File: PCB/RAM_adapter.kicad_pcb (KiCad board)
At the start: 2 copper layers, 78 x 64.5 mm, 18 parts, among them J1 #WR, J2 DB25_Plug, U1 HM62256BLP, U2 74LS573

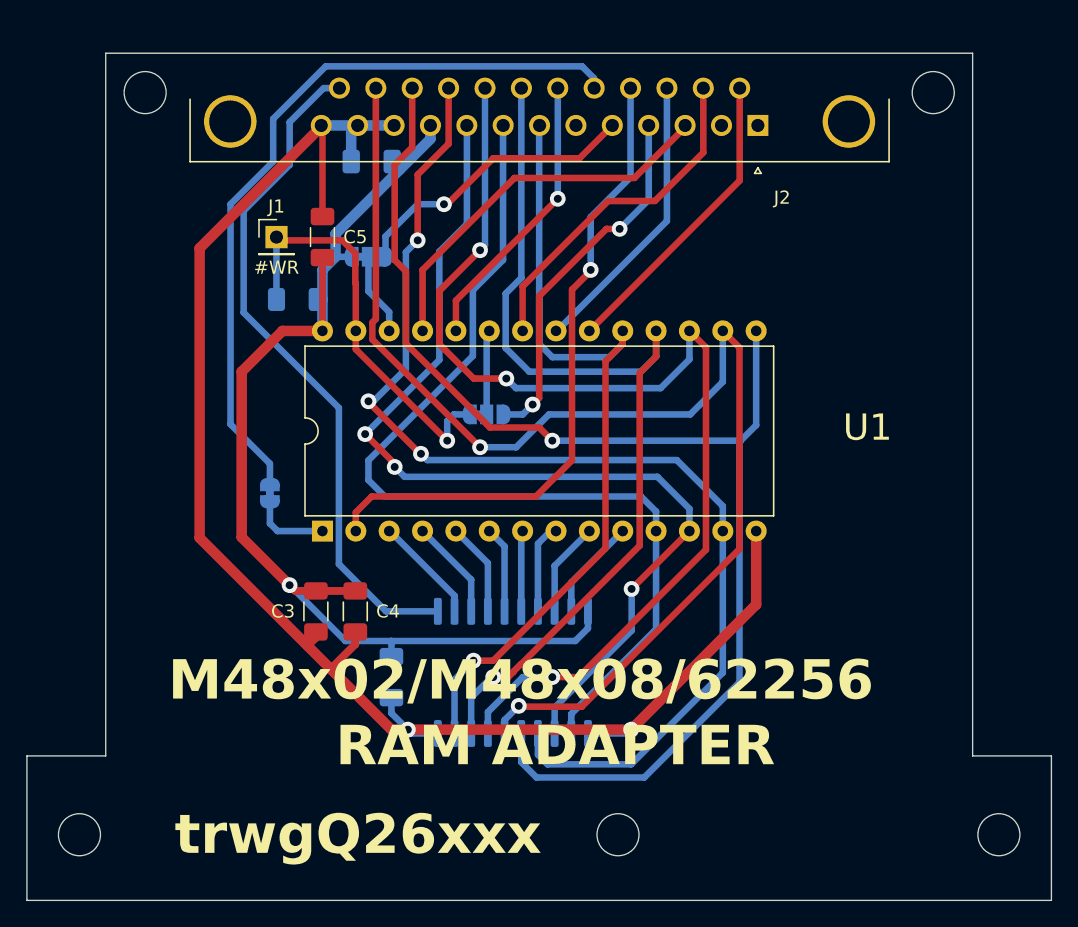
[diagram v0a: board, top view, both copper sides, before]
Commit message: Revised RAM adapter PCB
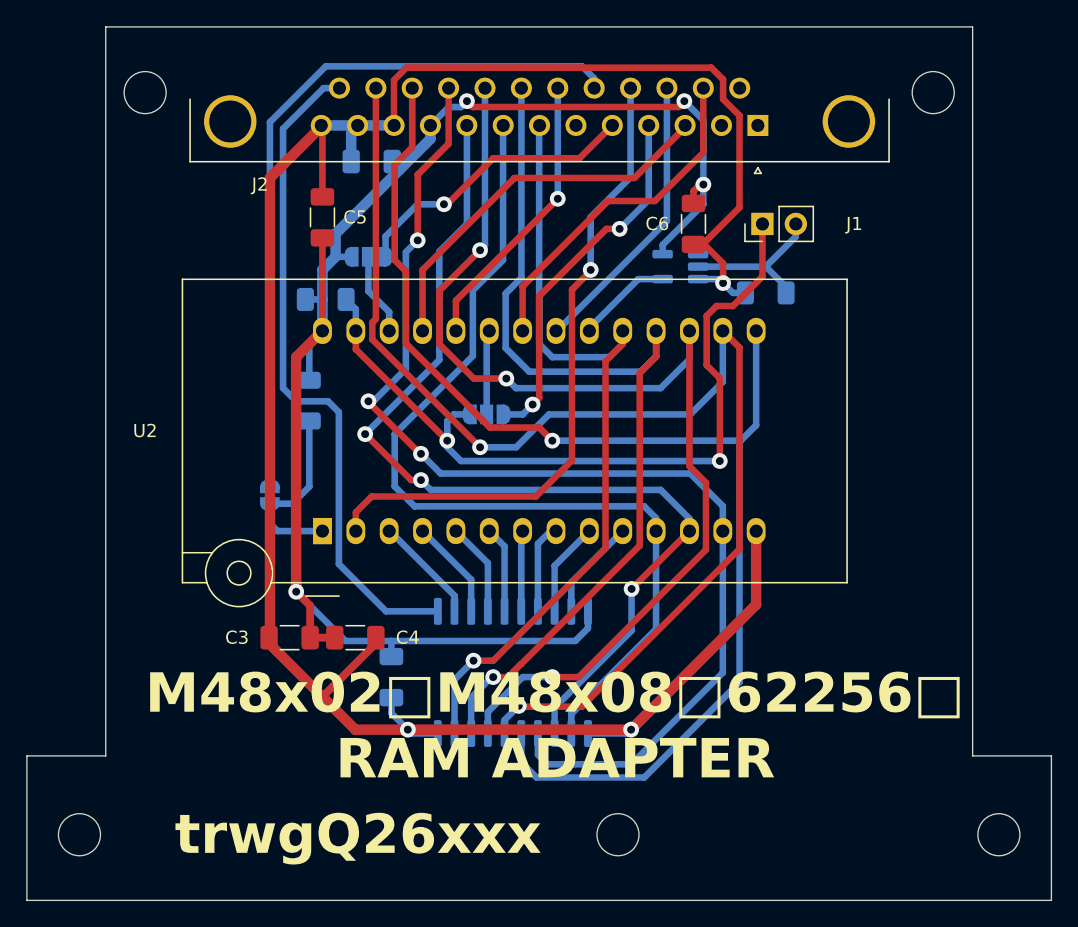
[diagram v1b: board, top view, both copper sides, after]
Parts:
- added C6: 100n, Capacitor_SMD:C_1206_3216Metric_Pad1.33x1.80mm_HandSolder, F.Cu at (166.8, 35.5)
- added R2: 10k, Resistor_SMD:R_1206_3216Metric_Pad1.30x1.75mm_HandSolder, B.Cu at (172.2, 40.8)
- added R3: 10k, Resistor_SMD:R_1206_3216Metric_Pad1.30x1.75mm_HandSolder, B.Cu at (137.5, 49.0)
- added U1: 74LVC1G04, Package_TO_SOT_SMD:SOT-23-5_HandSoldering, B.Cu at (165.8, 38.8)
- J1: value #WR -> EC; footprint Connector_PinHeader_2.54mm:PinHeader_1x01_P2.54mm_Vertical -> Connector_PinHeader_2.54mm:PinHeader_1x02_P2.54mm_Vertical
- JP1: footprint Jumper:SolderJumper-2_P1.3mm_Bridged_RoundedPad1.0x1.5mm -> Jumper:SolderJumper-2_P1.3mm_Open_RoundedPad1.0x1.5mm
- JP2, JP3: footprint Jumper:SolderJumper-3_P1.3mm_Bridged12_RoundedPad1.0x1.5mm_NumberLabels -> Jumper:SolderJumper-3_P1.3mm_Open_RoundedPad1.0x1.5mm
- U2: renamed from U1; footprint Package_DIP:DIP-28_W15.24mm -> Socket:DIP_Socket-28_W11.9_W12.7_W15.24_W17.78_W18.5_3M_228-1277-00-0602J
- moved J1 37.0 mm to (172.0, 35.5), turned to 90 degrees
- moved C3 2.83 mm to (136.0, 67.0), turned to 180 degrees
- moved R1 2.20 mm to (138.8, 41.2), turned to 0 degrees
- moved C4 2.00 mm to (141.0, 67.0), turned to 0 degrees
- moved C5 1.50 mm to (138.5, 35.0)
- moved JP1 0.15 mm to (134.5, 56.1)
- renumbered U2 to U3
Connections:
- J2 pad 14: #A -> unconnected-(J2-P14-Pad14)
- U2 pad 20: #A -> #CS
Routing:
- net GND: track 122.8 -> 171.4 mm, vias 2 -> 3
- net +5V: track 84.9 -> 122.7 mm, vias 1 -> 4
- net #WR: track 31.8 -> 60.3 mm, vias 1 -> 2
- net #A: track 23.2 -> 0.00 mm
- net A15: track 0.00 -> 12.0 mm
- net Net-(JP1-A): track 5.89 -> 14.4 mm
- net #CS: track 0.00 -> 7.34 mm
- net /D0: track 73.7 -> 70.9 mm
- net /A14: track 57.7 -> 55.2 mm
- net AS: track 52.0 -> 50.9 mm
- net /D1: track 75.3 -> 74.7 mm
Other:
- board size 78 x 64.5 mm -> 78 x 66.5 mm
- board text added: "M48x02□M48x08□62256□"
- board text added: "MT48x02/MT48x12: JP1 Don't care, JP2 1-2, JP3 1-2 MT48x08/MT48x18: JP1 OFF, JP2 1-2, JP3 2-3 62256: JP1 ON, JP2 2-3, JP3 2-3"
- board text removed: "M48x02/M48x08/62256"
- board text removed: "MT48x02/MT48x12: JP1 Don't care,JP2 1-2, JP3 1-2 MT48x08/MT48x18: JP1 OFF, JP2 1-2, JP3 2-3 62256: JP1 ON, JP2 2-3, JP3 2-3"

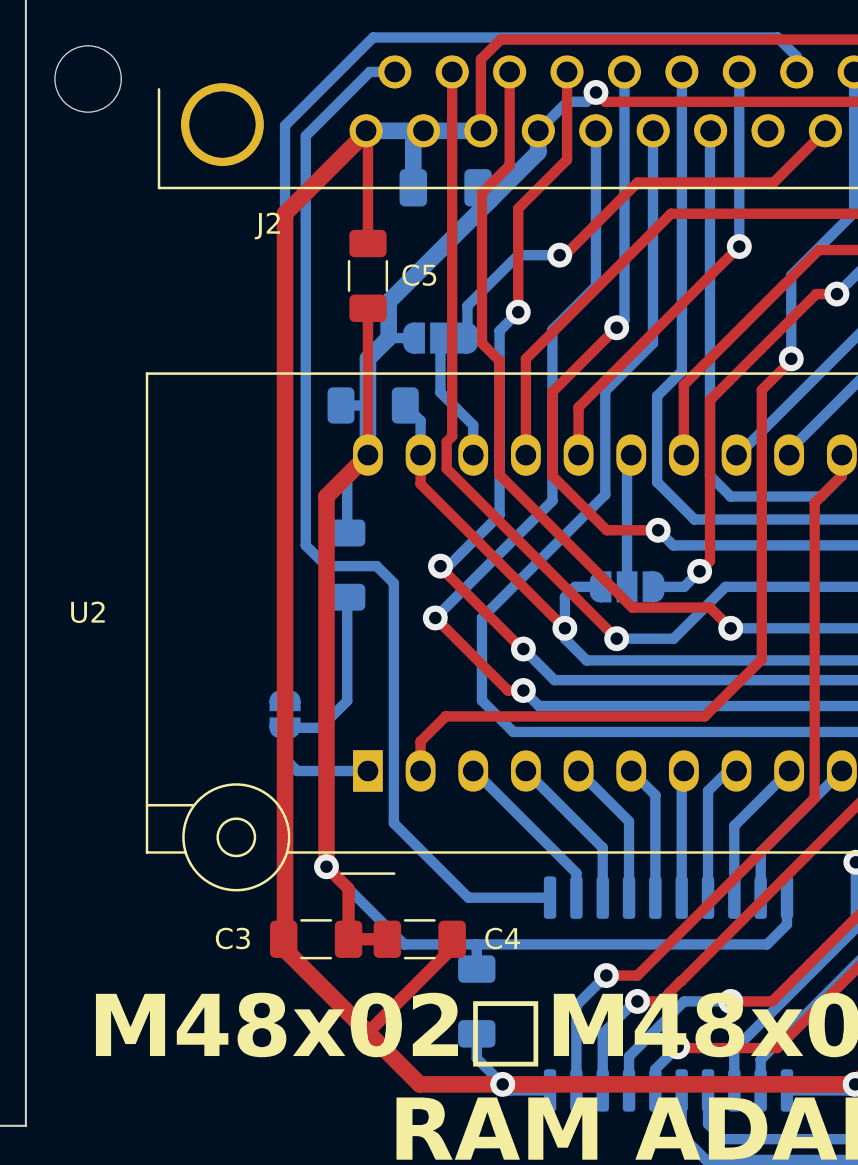
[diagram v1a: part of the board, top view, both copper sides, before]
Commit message: ROM reader project PCBs updated
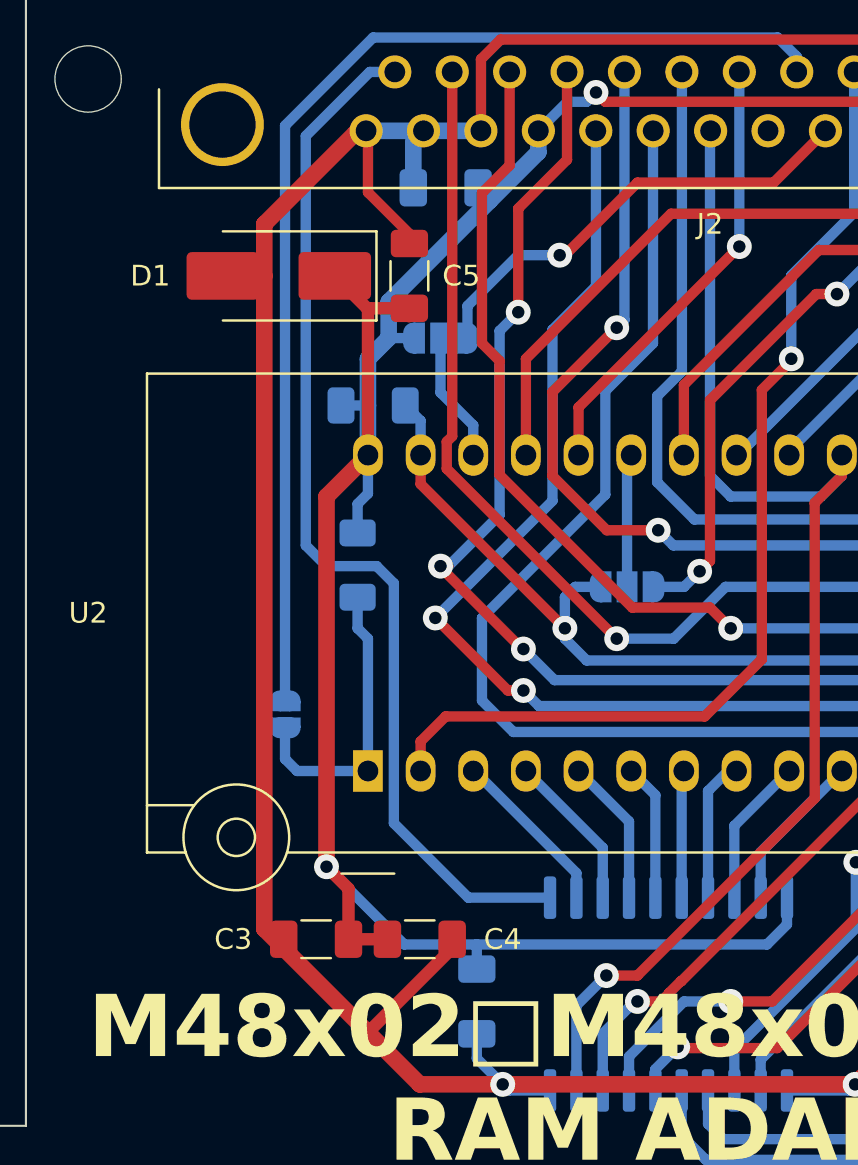
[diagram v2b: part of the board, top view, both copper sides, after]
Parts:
- added D1: Schottky, Diode_SMD:D_SMB_Handsoldering, F.Cu at (134.2, 35.0)
- moved C5 2.00 mm to (140.5, 35.0)
- moved R3 0.50 mm to (138.0, 49.0)
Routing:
- net +5V: track 122.7 -> 127.2 mm
- net GND: track 171.4 -> 175.4 mm
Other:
- board text added: "M48x02/M48x12: JP1 OFF, JP2 1-2, JP3 1-2 M48x08/M48x18: JP1 OFF, JP2 1-2, JP3 2-3 62256: JP1 ON, JP2 2-3, JP3 2-3"
- board text removed: "MT48x02/MT48x12: JP1 Don't care, JP2 1-2, JP3 1-2 MT48x08/MT48x18: JP1 OFF, JP2 1-2, JP3 2-3 62256: JP1 ON, JP2 2-3, JP3 2-3"

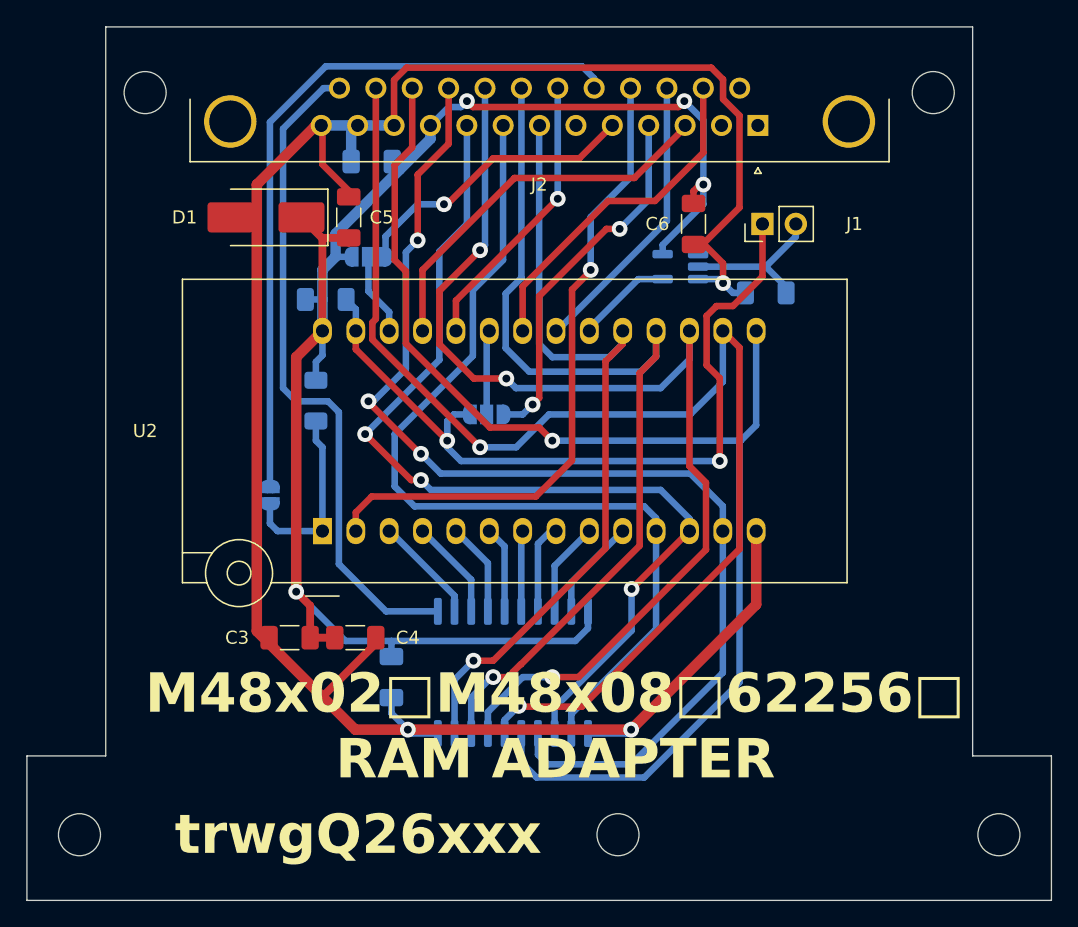
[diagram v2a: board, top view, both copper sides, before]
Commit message: Minor changes in text placement on PCB, comments. Revision updated to B
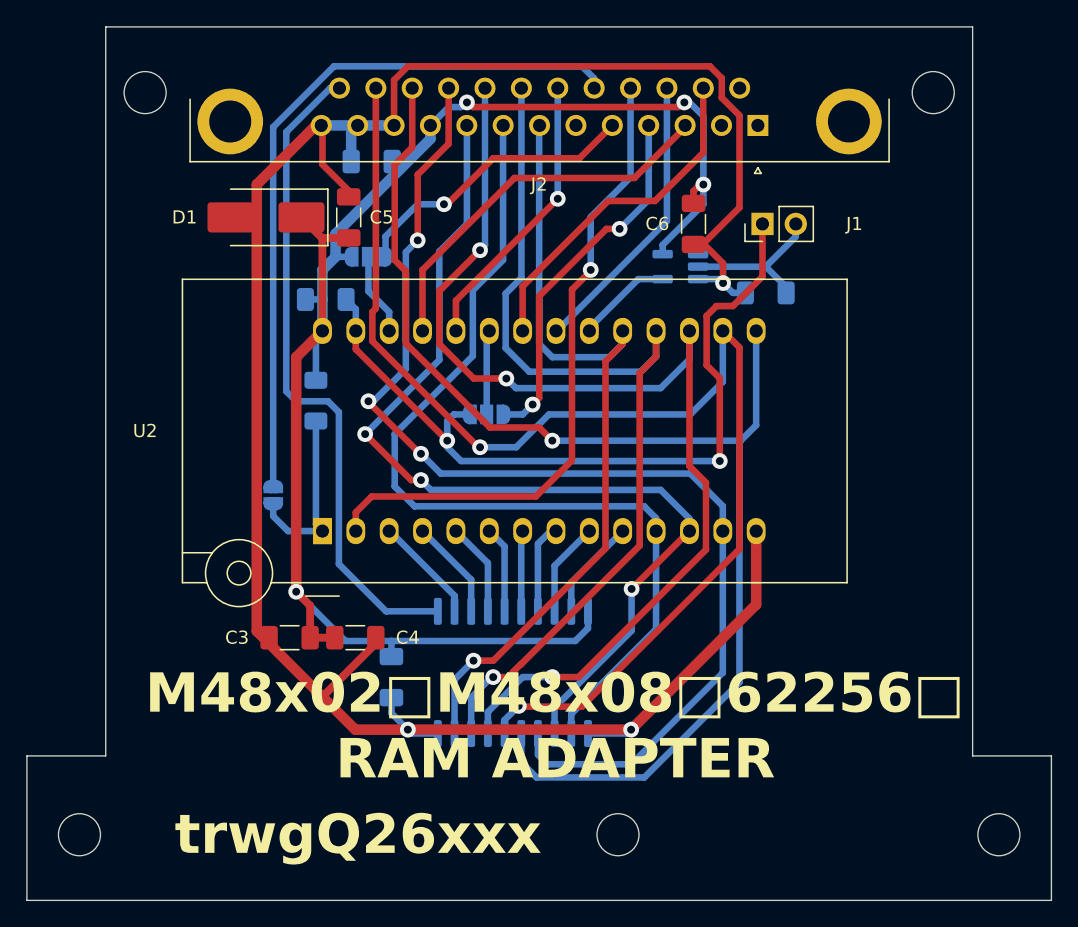
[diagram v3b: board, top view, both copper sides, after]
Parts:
- J1: value EC -> RAM ADAPTER EXT
- J2: value DB25_Plug -> ROM
- moved JP1 0.25 mm to (134.8, 56.1)
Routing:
- net Net-(JP1-A): track 14.5 -> 13.8 mm
- net AS: track 50.9 -> 50.4 mm
